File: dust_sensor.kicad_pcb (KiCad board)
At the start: 2 copper layers, 50 x 45 mm, 33 parts, among them P1 ADC, P10 PWR, P11 BMPx80, P2 POWER, P3 LCD, P4 EXP_INT, P5 SERIAL, P6 DHT, P7 SENSOR, P8 GPIOS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

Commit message: SCH: PCB: Add external I²C connector
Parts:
- added P12: I²C, Pin_Headers:Pin_Header_Angled_1x02_Pitch2.54mm, F.Cu at (86.2, 66.2)
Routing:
- net SDA: track 48.8 -> 53.9 mm
- net SCL: track 42.2 -> 47.4 mm
- net PROG: track 104.5 -> 108.0 mm

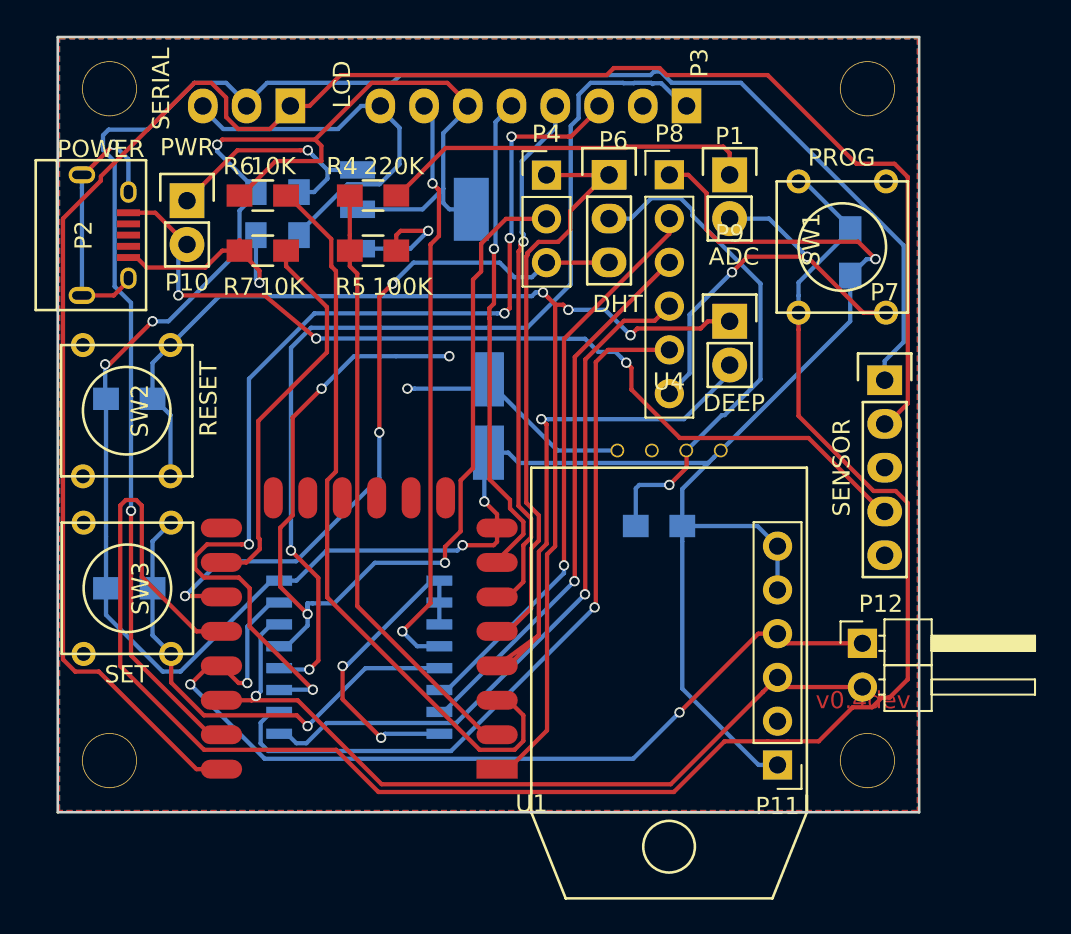
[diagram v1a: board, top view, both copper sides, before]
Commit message: PCB: SCH: add I²C pullups.
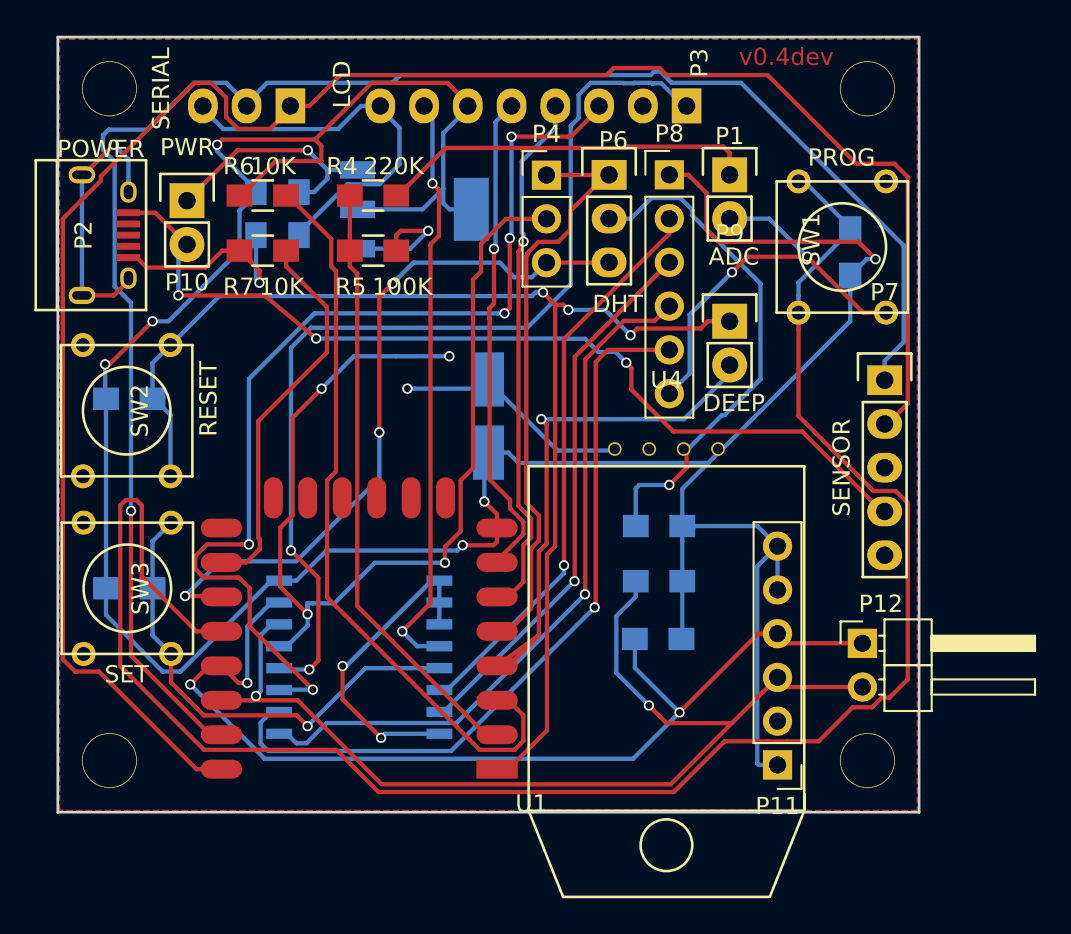
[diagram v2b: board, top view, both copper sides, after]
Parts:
- added R10: 4K7, Resistors_SMD:R_0805_HandSoldering, B.Cu at (74.4, 62.6)
- added R9: 4K7, Resistors_SMD:R_0805_HandSoldering, B.Cu at (74.3, 65.9)
- moved U4 0.17 mm to (74.8, 53.9)
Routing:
- net SCL: track 47.4 -> 61.0 mm, vias 1 -> 2
- net SDA: track 53.9 -> 59.3 mm
- net +3V3: track 176.7 -> 180.8 mm

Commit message: PCB: small clenups
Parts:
- SW1, SW2, SW3: moved to B.Cu
- turned SW1 to 270 degrees
- turned SW2 to 90 degrees
- turned SW3 to 90 degrees
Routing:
- net Net-(P4-Pad2): track 59.7 -> 36.2 mm, vias 4 -> 1
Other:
- board text added: "G"
- board text added: "R"
- board text added: "SCL"
- board text added: "SDA"
- board text added: "T"

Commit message: PCB: traces optimalization
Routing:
- net GND: track 101.1 -> 218.4 mm, vias 7 -> 5
- net PROG: track 108.0 -> 93.6 mm
- net SET: track 28.2 -> 36.4 mm, vias 1 -> 0
- net RESET: track 72.4 -> 77.2 mm, vias 3 -> 2
- net GPIO16: track 31.5 -> 35.9 mm, vias 1 -> 0
- net Net-(R6-Pad1): track 43.4 -> 40.2 mm
- net SDA: track 59.3 -> 56.5 mm, vias 3 -> 1
- net Net-(R7-Pad1): track 22.5 -> 20.8 mm
- net Net-(P3-Pad3): track 59.6 -> 58.1 mm, vias 5 -> 1
- net Net-(P3-Pad1): track 58.3 -> 59.3 mm
- net +5V: track 54.9 -> 54.2 mm
- net LIGHT: track 34.2 -> 33.6 mm
- net P2: track 33.3 -> 33.8 mm
